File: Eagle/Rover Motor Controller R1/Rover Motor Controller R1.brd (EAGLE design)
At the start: 12.7 x 25.4 mm, 14 parts, among them U1 ATTINY2313A

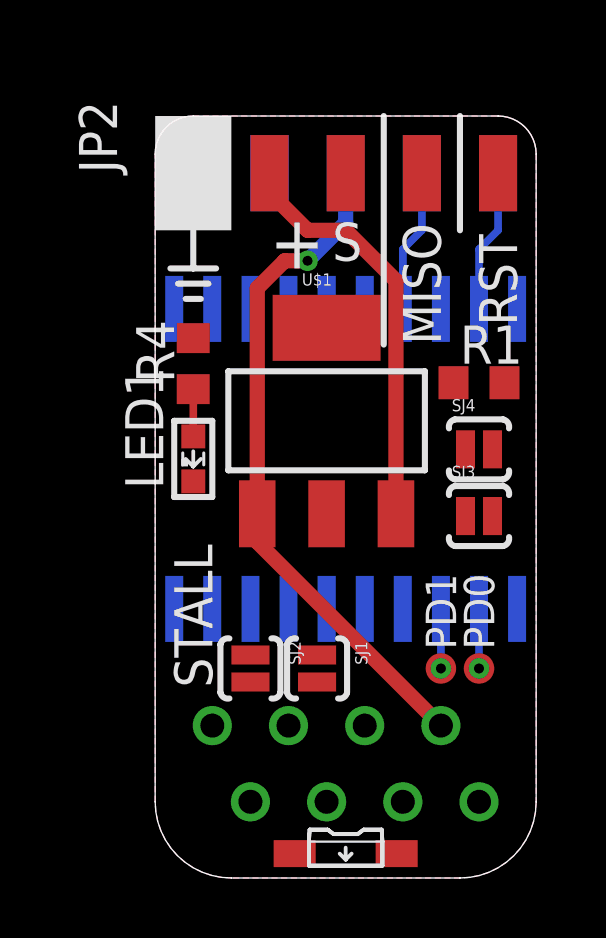
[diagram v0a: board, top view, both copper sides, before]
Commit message: New Motor Controller Revision
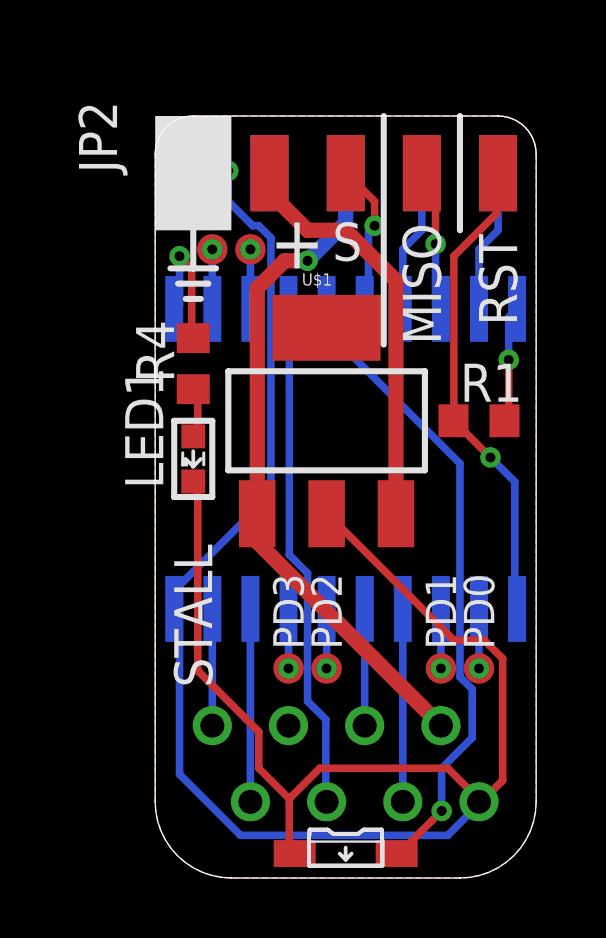
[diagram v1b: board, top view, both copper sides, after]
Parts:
- removed SJ1, SJ2, SJ3, SJ4: JUMPER-PAD-2-NOYES_SILK, SparkFun-Passives:PAD-JUMPER-2-NO_YES_SILK
- added TP3, TP4, TP5, TP6: TEST-POINT3X4, SparkFun-Passives:PAD.03X.04
- moved R1 1.27 mm to (10.8, 15.2)
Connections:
- removed net PD4: SJ1.1, U1.8
- removed net PD5: SJ2.1, U1.9
- new net PD2: TP3.P$1, U1.6
- new net PD3: TP4.P$1, U1.7
- net GND: no longer SJ1.2, SJ2.2, SJ3.2, SJ4.2
- net PB0: now also TP5.P$1; no longer SJ3.1
- net PB1: now also TP6.P$1; no longer SJ4.1
- net QEA: now also U1.8; no longer U1.6
- net QEB: now also U1.9; no longer U1.7
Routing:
- net GND: track 0.00 -> 70.2 mm, vias 0 -> 1
- net LAMP: track 0.00 -> 21.3 mm, vias 0 -> 1
- net PWM: track 0.00 -> 16.9 mm
- net RST: track 0.00 -> 16.0 mm, vias 0 -> 1
- net QEA: track 0.00 -> 6.43 mm
- net IN1: track 0.00 -> 6.43 mm
- net SERVO: track 0.00 -> 5.07 mm, vias 0 -> 1
- net MISO: track 0.00 -> 4.79 mm, vias 0 -> 1
- net STALL: track 0.00 -> 4.76 mm, vias 0 -> 1
- net +3V3: track 0.00 -> 3.99 mm, vias 0 -> 1
- net QEB: track 0.00 -> 3.89 mm
- net IN2: track 0.00 -> 3.89 mm
- net PD3: track 0.00 -> 1.99 mm, vias 0 -> 1
- net PD2: track 0.00 -> 1.99 mm, vias 0 -> 1
- net PB1: track 0.00 -> 1.98 mm, vias 0 -> 1
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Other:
- board text added: "141001"
- board text added: "PD2"
- board text added: "PD3"
- board text removed: "141015"
